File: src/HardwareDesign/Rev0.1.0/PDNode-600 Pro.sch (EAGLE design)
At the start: 652 parts, among them IC1 AP22653W6, IC11 STUSB4710, IC12 TPS552882, IC13 INA219BIDCNT, IC14 STUSB4710, IC15 TPS552882, IC16 INA219BIDCNT, IC17 STUSB4710, IC18 TPS552882, IC19 INA219BIDCNT, IC2 AP22653W6, IC20 STUSB4710, IC21 TPS552882, IC22 INA219BIDCNT, IC23 STUSB4710, IC24 TPS552882, IC25 INA219BIDCNT, IC26 RP2040, IC27 W25Q128JVPIQ, IC28 MCP6001R, IC29 CAT24C512HU5IGT3, IC3 AP22653W6, IC31 STUSB4710, IC32 TPS552882, IC33 INA219BIDCNT, IC34 STUSB4710, IC35 TPS552882, IC36 INA219BIDCNT, IC37 STUSB4710, IC38 TCA9548ARGER, IC39 W5500, IC4 SN74LVC1G04DBVR, IC40 MP2315S, IC41 TPS552882, IC42 MCP23017-E/ML, IC43 MP2315S, IC44 INA219BIDCNT, IC45 MP2315S, IC5 SN74LVC1G04DBVR, IC6 SN74LVC1G04DBVR, IC7 SN74LVC1G04DBVR, IC8 AP22653W6, J8 691244510006, T10 IPZ40N04S5L2R8, T11 DMP3013SFV, T12 DMP3013SFV, T13 DMP3013SFV, T14 IPZ40N04S5L-7R4, T15 IPZ40N04S5L2R8, T16 DMP3013SFV, T17 DMP3013SFV, T18 DMP3013SFV, T19 IPZ40N04S5L-7R4, T20 IPZ40N04S5L2R8, T21 DMP3013SFV, T22 DMP3013SFV, T23 DMP3013SFV, T24 IPZ40N04S5L-7R4, T25 IPZ40N04S5L2R8, T26 DMP3013SFV, T27 DMP3013SFV, T28 DMP3013SFV, T29 IPZ40N04S5L-7R4, T30 IPZ40N04S5L2R8, T31 DMP3013SFV, T32 DMP3013SFV, T33 DMP3013SFV, T34 IPZ40N04S5L-7R4, T35 IPZ40N04S5L2R8, T36 DMP3013SFV, T37 DMP3013SFV, T38 DMP3013SFV, T39 IPZ40N04S5L-7R4, T40 IPZ40N04S5L2R8, T41 DMP3013SFV, T42 DMP3013SFV, T43 DMP3013SFV, T44 IPZ40N04S5L-7R4, T45 IPZ40N04S5L2R8, T6 DMP3013SFV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

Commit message: Hardware design update
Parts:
- removed IC31, IC34, IC37: STUSB4710, ds_ic_peripherals:STUSB4710
- added IC10, IC30, IC9: STUSB4710AQ1TR, ds_ic_peripherals:STUSB4710AQ1TR
- IC1, IC2, IC3, IC8: value AP22653W6 -> AP22653W6-7
- IC11, IC14, IC17, IC20, IC23: value STUSB4710 -> STUSB4710AQ1TR; device ds_ic_peripherals:STUSB4710 -> ds_ic_peripherals:STUSB4710AQ1TR
- T10, T15, T20, T25, T30, T35, T40, T45: value IPZ40N04S5L2R8 -> BSZ065N06LS5ATMA1
- T14, T19, T24, T29, T34, T39, T44, T9: value IPZ40N04S5L-7R4 -> BSZ065N06LS5ATMA1
- X1: value 12MHz -> X322512MSB4SI
- X2: value 25MHz -> X322525MOB4SI; device crystal-geyer_V1_0:KX-7 -> Wurth_Quartz Crystals & Oscillators_WE-XTAL:WE-XTAL_CFPX-180_830035268
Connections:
- net CC1_PORT1: now also IC9.CC1; no longer IC11.CC1
- net CC1_PORT2: now also IC10.CC1; no longer IC14.CC1
- net CC1_PORT3: now also IC11.CC1; no longer IC23.CC1
- net CC1_PORT4: now also IC14.CC1; no longer IC20.CC1
- net CC1_PORT6: now also IC20.CC1; no longer IC31.CC1
- net CC1_PORT7: now also IC23.CC1; no longer IC34.CC1
- net CC1_PORT8: now also IC30.CC1; no longer IC37.CC1
- net CC2_PORT1: now also IC9.CC2; no longer IC11.CC2
- net CC2_PORT2: now also IC10.CC2; no longer IC14.CC2
- net CC2_PORT3: now also IC11.CC2; no longer IC23.CC2
- net CC2_PORT4: now also IC14.CC2; no longer IC20.CC2
- net CC2_PORT6: now also IC20.CC2; no longer IC31.CC2
- net CC2_PORT7: now also IC23.CC2; no longer IC34.CC2
- net CC2_PORT8: now also IC30.CC2; no longer IC37.CC2
- net GND: now also IC10.GND, IC30.GND, IC9.GND, X2.GND; no longer IC11.PAD, IC14.PAD, IC17.PAD, IC20.PAD, IC23.PAD, IC31.GND, IC31.PAD, IC34.GND, IC34.PAD, IC37.GND, IC37.PAD
- net IN1_PORT1: now also IC9.VBUS_SENSE; no longer IC11.VBUS_SENSE
- net IN1_PORT2: now also IC10.VBUS_SENSE; no longer IC14.VBUS_SENSE
- net IN1_PORT3: now also IC11.VBUS_SENSE; no longer IC23.VBUS_SENSE
- net IN1_PORT4: now also IC14.VBUS_SENSE; no longer IC20.VBUS_SENSE
- net IN1_PORT6: now also IC20.VBUS_SENSE; no longer IC31.VBUS_SENSE
- net IN1_PORT7: now also IC23.VBUS_SENSE; no longer IC34.VBUS_SENSE
- net IN1_PORT8: now also IC30.VBUS_SENSE; no longer IC37.VBUS_SENSE
- net N$135: now also IC14.SEL_PDO5; no longer IC20.SEL_PDO5
- net N$136: now also IC14.SEL_PDO4; no longer IC20.SEL_PDO4
- net N$137: now also IC14.SEL_PDO3; no longer IC20.SEL_PDO3
- net N$138: now also IC14.SEL_PDO2; no longer IC20.SEL_PDO2
- net N$139: now also IC14.VREG1V2; no longer IC20.VREG1V2
- net N$140: now also IC14.VREG2V7; no longer IC20.VREG2V7
- net N$141: now also IC14.ADDR0; no longer IC20.ADDR0
- net N$143: now also IC14.VBUS_DISCH; no longer IC20.VBUS_DISCH
- net N$146: now also IC14.VBUS_EN_SRC; no longer IC20.VBUS_EN_SRC
- net N$164: now also IC11.SEL_PDO5; no longer IC23.SEL_PDO5
- net N$165: now also IC11.SEL_PDO4; no longer IC23.SEL_PDO4
- net N$166: now also IC11.SEL_PDO3; no longer IC23.SEL_PDO3
- net N$167: now also IC11.SEL_PDO2; no longer IC23.SEL_PDO2
- net N$168: now also IC11.VREG1V2; no longer IC23.VREG1V2
- net N$169: now also IC11.VREG2V7; no longer IC23.VREG2V7
- net N$170: now also IC11.ADDR0; no longer IC23.ADDR0
- net N$172: now also IC11.VBUS_DISCH; no longer IC23.VBUS_DISCH
- net N$175: now also IC11.VBUS_EN_SRC; no longer IC23.VBUS_EN_SRC
- net N$193: now also IC20.SEL_PDO5; no longer IC31.SEL_PDO5
- net N$194: now also IC20.SEL_PDO4; no longer IC31.SEL_PDO4
- net N$195: now also IC20.SEL_PDO3; no longer IC31.SEL_PDO3
- net N$196: now also IC20.SEL_PDO2; no longer IC31.SEL_PDO2
- net N$197: now also IC20.VREG1V2; no longer IC31.VREG1V2
- net N$198: now also IC20.VREG2V7; no longer IC31.VREG2V7
- net N$199: now also IC20.ADDR0; no longer IC31.ADDR0
- net N$201: now also IC20.VBUS_DISCH; no longer IC31.VBUS_DISCH
- net N$204: now also IC20.VBUS_EN_SRC; no longer IC31.VBUS_EN_SRC
- net N$223: now also IC23.SEL_PDO5; no longer IC34.SEL_PDO5
- net N$224: now also IC23.SEL_PDO4; no longer IC34.SEL_PDO4
- net N$225: now also IC23.SEL_PDO3; no longer IC34.SEL_PDO3
- net N$226: now also IC23.SEL_PDO2; no longer IC34.SEL_PDO2
- net N$227: now also IC23.VREG1V2; no longer IC34.VREG1V2
- net N$228: now also IC23.VREG2V7; no longer IC34.VREG2V7
- net N$229: now also IC23.ADDR0; no longer IC34.ADDR0
- net N$231: now also IC23.VBUS_DISCH; no longer IC34.VBUS_DISCH
- net N$234: now also IC23.VBUS_EN_SRC; no longer IC34.VBUS_EN_SRC
- net N$253: now also IC30.SEL_PDO5; no longer IC37.SEL_PDO5
- net N$254: now also IC30.SEL_PDO4; no longer IC37.SEL_PDO4
- net N$255: now also IC30.SEL_PDO3; no longer IC37.SEL_PDO3
- net N$256: now also IC30.SEL_PDO2; no longer IC37.SEL_PDO2
- net N$262: now also IC30.VREG1V2; no longer IC37.VREG1V2
- net N$263: now also IC30.VREG2V7; no longer IC37.VREG2V7
- net N$264: now also IC30.ADDR0; no longer IC37.ADDR0
- net N$266: now also IC30.VBUS_DISCH; no longer IC37.VBUS_DISCH
- net N$274: now also IC30.VBUS_EN_SRC; no longer IC37.VBUS_EN_SRC
- net N$48: now also IC9.SEL_PDO5; no longer IC11.SEL_PDO5
- net N$49: now also IC9.SEL_PDO4; no longer IC11.SEL_PDO4
- net N$50: now also IC9.SEL_PDO3; no longer IC11.SEL_PDO3
- net N$51: now also IC9.SEL_PDO2; no longer IC11.SEL_PDO2
- net N$52: now also IC9.VREG1V2; no longer IC11.VREG1V2
- net N$53: now also IC9.VREG2V7; no longer IC11.VREG2V7
- net N$54: now also IC9.ADDR0; no longer IC11.ADDR0
- net N$56: now also IC9.VBUS_DISCH; no longer IC11.VBUS_DISCH
- net N$59: now also IC9.VBUS_EN_SRC; no longer IC11.VBUS_EN_SRC
- net N$77: now also IC10.SEL_PDO5; no longer IC14.SEL_PDO5
- net N$78: now also IC10.SEL_PDO4; no longer IC14.SEL_PDO4
- net N$79: now also IC10.SEL_PDO3; no longer IC14.SEL_PDO3
- net N$80: now also IC10.SEL_PDO2; no longer IC14.SEL_PDO2
- net N$81: now also IC10.VREG1V2; no longer IC14.VREG1V2
- net N$82: now also IC10.VREG2V7; no longer IC14.VREG2V7
- net N$83: now also IC10.ADDR0; no longer IC14.ADDR0
- net N$85: now also IC10.VBUS_DISCH; no longer IC14.VBUS_DISCH
- net N$88: now also IC10.VBUS_EN_SRC; no longer IC14.VBUS_EN_SRC
- net TCA0_I2C_SCL: now also IC10.SCL, IC9.SCL; no longer IC11.SCL, IC14.SCL
- net TCA0_I2C_SDA: now also IC10.SDA, IC9.SDA; no longer IC11.SDA, IC14.SDA
- net TCA1_I2C_SCL: now also IC11.SCL, IC14.SCL; no longer IC20.SCL, IC23.SCL
- net TCA1_I2C_SDA: now also IC11.SDA, IC14.SDA; no longer IC20.SDA, IC23.SDA
- net TCA2_I2C_SCL: now also IC20.SCL; no longer IC31.SCL
- net TCA2_I2C_SDA: now also IC20.SDA; no longer IC31.SDA
- net TCA3_I2C_SCL: now also IC23.SCL, IC30.SCL; no longer IC34.SCL, IC37.SCL
- net TCA3_I2C_SDA: now also IC23.SDA, IC30.SDA; no longer IC34.SDA, IC37.SDA
- net VSRC1: now also IC9.VDD; no longer IC11.VDD
- net VSRC2: now also IC10.VDD; no longer IC14.VDD
- net VSRC3: now also IC11.VDD; no longer IC23.VDD
- net VSRC4: now also IC14.VDD; no longer IC20.VDD
- net VSRC6: now also IC20.VDD; no longer IC31.VDD
- net VSRC7: now also IC23.VDD; no longer IC34.VDD
- net VSRC8: now also IC30.VDD; no longer IC37.VDD
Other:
- moved on the sheet: C219

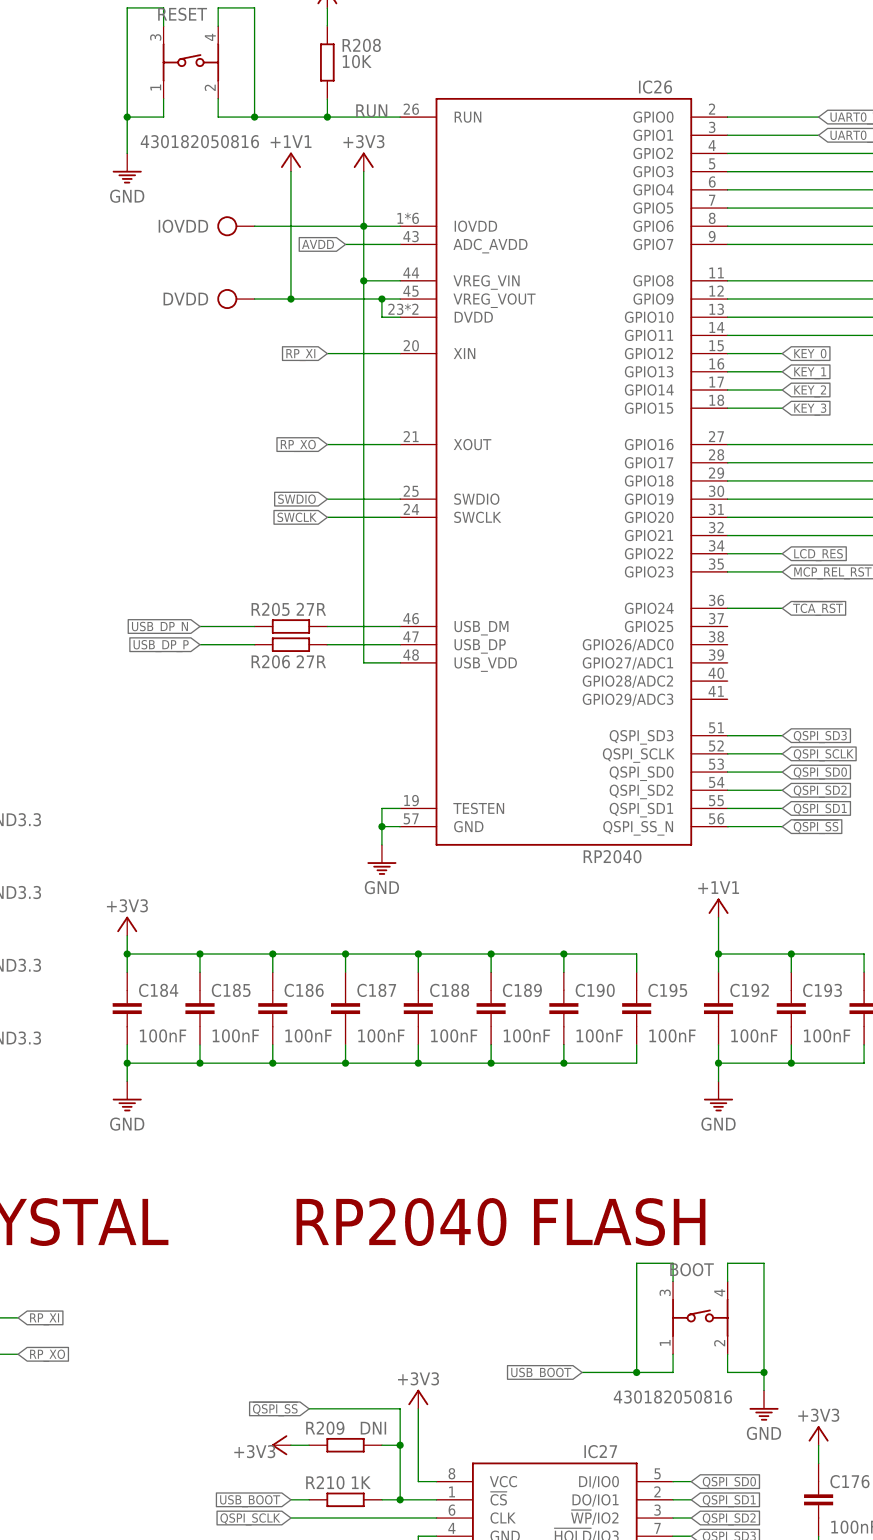
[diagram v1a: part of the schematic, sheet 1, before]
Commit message: Update RESET and BOOT part values in hardware design files
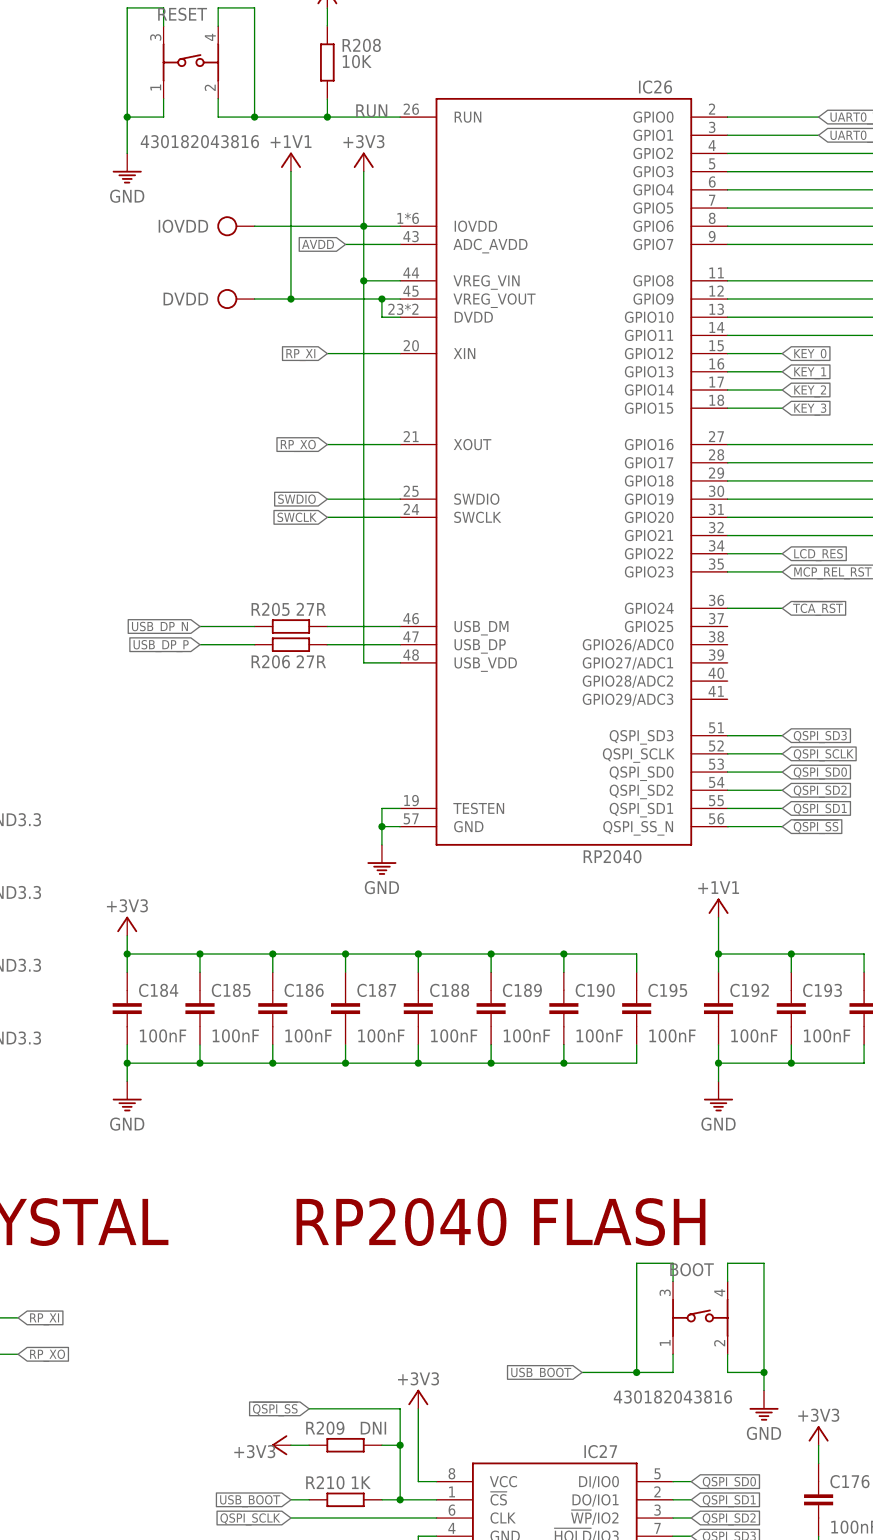
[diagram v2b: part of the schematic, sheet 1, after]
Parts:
- BOOT, RESET: value 430182050816 -> 430182043816
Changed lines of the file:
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@@
 <part name="R208" library="ds_passive" deviceset="R" device="0201" package3d_urn="urn:adsk.eagle:package:47403529/3" value="10K"/>
 <part name="+3V24" library="ds_passive" deviceset="+3V3" device=""/>
-<part name="RESET" library="Wurth_Switch_WS-TASV" library_urn="urn:adsk.eagle:library:18304196" deviceset="430182050816" device="" package3d_urn="urn:adsk.eagle:package:18304299/2" value="430182050816"/>
+<part name="RESET" library="Wurth_Switch_WS-TASV" library_urn="urn:adsk.eagle:library:18304196" deviceset="430182050816" device="" package3d_urn="urn:adsk.eagle:package:18304299/2" value="430182043816"/>
 <part name="IC27" library="ds_ic_memory" deviceset="W25Q128JV" device="P" package3d_urn="urn:adsk.eagle:package:45369668/1" value="W25Q128JVPIQ"/>
 <part name="R209" library="ds_passive" deviceset="R" device="0201" package3d_urn="urn:adsk.eagle:package:47403529/3" value="DNI"/>
@@
 <part name="GND215" library="ds_passive" deviceset="GND" device=""/>
 <part name="X1" library="Wurth_Quartz Crystals &amp; Oscillators_WE-XTAL" library_urn="urn:adsk.eagle:library:14284023" deviceset="WE-XTAL_CFPX-180" device="" package3d_urn="urn:adsk.eagle:package:13029090/2" technology="_830055295" value="X322512MSB4SI"/>
-<part name="BOOT" library="Wurth_Switch_WS-TASV" library_urn="urn:adsk.eagle:library:18304196" deviceset="430182050816" device="" package3d_urn="urn:adsk.eagle:package:18304299/2" value="430182050816"/>
+<part name="BOOT" library="Wurth_Switch_WS-TASV" library_urn="urn:adsk.eagle:library:18304196" deviceset="430182050816" device="" package3d_urn="urn:adsk.eagle:package:18304299/2" value="430182043816"/>
 <part name="REF1" library="ds_ic_vreg" deviceset="LM4040BXX" device="" package3d_urn="urn:adsk.eagle:package:46684430/3"/>
 <part name="GND216" library="ds_passive" deviceset="GND" device=""/>
